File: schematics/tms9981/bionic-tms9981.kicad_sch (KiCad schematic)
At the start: 8 parts, among them J1 Bionic-P135, J2 Bionic-P245, U1 TMS9981, U2 11AA010-I/TT

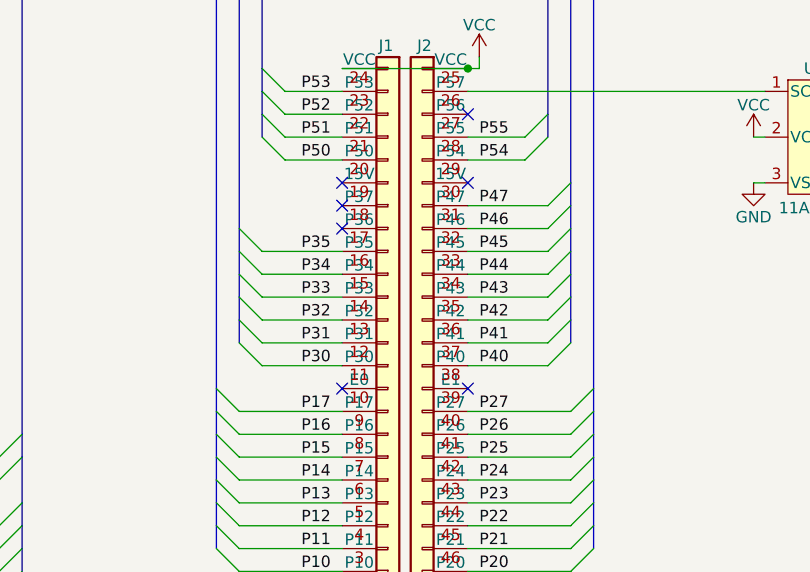
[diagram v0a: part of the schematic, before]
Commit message: [TMS9981] Cleanup schematics
Remove LDO version
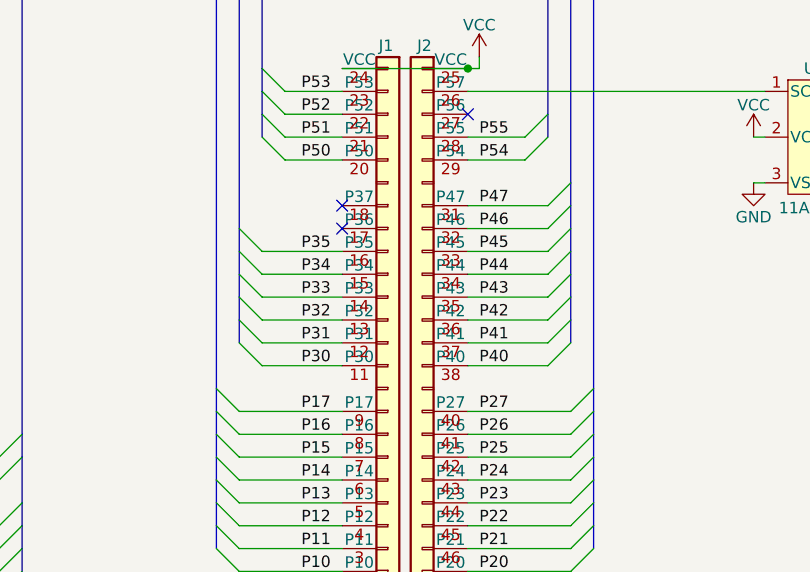
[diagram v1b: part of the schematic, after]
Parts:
- J1: footprint bionic:Bionic-P135_Vertical -> bionic:Bionic-P135_THT
- J2: footprint bionic:Bionic-P245_Vertical -> bionic:Bionic-P245_THT
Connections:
- no-connect marks 8 -> 4
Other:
- title: BionicTMS9981 DC/DC -> BionicTMS9981
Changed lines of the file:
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@@
 	(paper "A4")
 	(title_block
-		(title "BionicTMS9981 DC/DC")
-		(date "2025-02-10")
-		(rev "3")
+		(title "BionicTMS9981")
+		(date "2025-03-02")
+		(rev "4")
 		(company "Tadashi G. Takaoka")
 	)
@@
 	)
 	(no_connect
-		(at 157.48 100.33)
-	)
-	(no_connect
-		(at 157.48 77.47)
-	)
-	(no_connect
 		(at 171.45 69.85)
 	)
 	(no_connect
-		(at 171.45 77.47)
-	)
-	(no_connect
 		(at 85.09 113.03)
 	)
@@
 	)
 	(no_connect
-		(at 171.45 100.33)
-	)
-	(no_connect
 		(at 157.48 80.01)
 	)
@@
 			)
 		)
-		(property "Footprint" "bionic:Bionic-P245_Vertical"
+		(property "Footprint" "bionic:Bionic-P245_THT"
 			(at 171.45 128.27 0)
 			(effects
@@
 		(pin "44"
 		)
-		(pin "39"
-		)
 		(pin "40"
 		)
@@
 		(pin "29"
 		)
-		(pin "30"
-		)
 		(pin "36"
 		)
@@
 			)
 		)
-		(property "Footprint" "bionic:Bionic-P135_Vertical"
+		(property "Footprint" "bionic:Bionic-P135_THT"
 			(at 163.83 128.27 0)
 			(effects
@@
 		(pin "21"
 		)
-		(pin "10"
-		)
 		(pin "1"
 		)
@@
 		(pin "23"
 		)
-		(pin "19"
-		)
 		(pin "15"
 		)
@@
 		)
 		(instances
-			(project "bionic-tms9981-dcdc"
+			(project "bionic-tms9981"
 				(path "/32fd0672-b7dc-4fee-9c81-67a8a5714b24"
 					(page "2")
